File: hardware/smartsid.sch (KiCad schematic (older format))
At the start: 48 parts, among them P1 INPUT, P2 CONTROL, P3 POT2, P4 SOCKET, P5 OUTPUT, U1 GAL16V8, U2 SID2, U3 7812, U4 7809, U5 SID1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

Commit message: Hardware: Added digifix again, rearranged components, rerouted
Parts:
- removed JP8: NR2, Pin_Headers:Pin_Header_Straight_1x02, symbol JUMPER
- removed P2: CONTROL, Pin_Headers:Pin_Header_Straight_1x06, symbol CONN_01X06
- removed R1: 100k, Discret:R1, symbol R_Small
- added C19: 10n, Capacitors_ThroughHole:C_Disc_D3_P2.5, symbol C
- added JP10: NR2, Pin_Headers:Pin_Header_Straight_1x02, symbol JUMPER
- added JP11: INPUT1, Pinheaders:Pin_Header_Straight_1x03, symbol JUMPER3
- added JP8: INPUT2, Pinheaders:Pin_Header_Straight_1x03, symbol JUMPER3
- added P2: CONTROL, Pin_Headers:Pin_Header_Straight_2x03, symbol CONN_02X03
- added R1, R10: 220, Discret:R1, symbol R
- added R9: 100k, Discret:R1, symbol R_Small
- added RV1, RV2: 1M, Potentiometers:Potentiometer_Trimmer-Suntan-TSR-3386C, symbol POT
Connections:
- net labels added: S1IN, S2IN
- wire segments 80 -> 82
- no-connect marks 8 -> 10
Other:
- moved on the sheet: C14, C15, C16, C17, C18, JP9, R2, R3, R4, R5, R6, R7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

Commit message: Hardware: Now using original output circuits instead of opamp
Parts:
- removed C15, C16: 2.2u, Capacitors_ThroughHole:C_Disc_D3_P2.5, symbol C_Small
- removed U7: OPA2132, Housings_DIP:DIP-8_W7.62mm, symbol TL072
- added C15, C20: 1000p, Capacitors_ThroughHole:C_Disc_D3_P2.5, symbol C
- added C16, C21: 470p, Capacitors_ThroughHole:C_Disc_D3_P2.5, symbol C
- added C22: 10u, Capacitors_ThroughHole:C_Radial_D5_L6_P2.5, symbol C
- added Q1, Q2: Q_NPN_BCE, TO_SOT_Packages_THT:TO-92_Inline_Narrow_Oval, symbol Q_NPN_BCE
- added R11: 10k, Discret:R1, symbol R
- added R12: 1k, Discret:R1, symbol R
- C19: value 10n -> 10u; footprint Capacitors_ThroughHole:C_Disc_D3_P2.5 -> Capacitors_ThroughHole:C_Radial_D5_L6_P2.5
- R4: value 47k -> 10k
- R6: value 47k -> 1k
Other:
- moved on the sheet: C13, C14, JP10, JP11, JP8, JP9, R1, R10, R2, R9, RV1, RV2

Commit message: Hardware: Use pin headers instead of dip socket for the sid socket
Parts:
- removed P4: SOCKET, Housings_DIP:DIP-28_W15.24mm, symbol CONN_01X28
- added P4: SOCKET LEFT, Pin_Headers:Pin_Header_Straight_1x14, symbol CONN_01X14
- added P6: SOCKET RIGHT, Pin_Headers:Pin_Header_Straight_1x14, symbol CONN_01X14
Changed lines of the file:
@@
 	1    0    0    -1
 $EndComp
-$Comp
-L CONN_01X28 P4
-U 1 1 56D96DFF
-P 1250 5550
-F 0 "P4" H 1250 7000 50  0000 C CNN
-F 1 "SOCKET" V 1350 5550 50  0000 C CNN
-F 2 "Housings_DIP:DIP-28_W15.24mm" H 1250 5550 60  0001 C CNN
-F 3 "" H 1250 5550 60  0000 C CNN
-	1    1250 5550
-	1    0    0    -1
-$EndComp
-NoConn ~ 1050 4200
-NoConn ~ 1050 4300
-NoConn ~ 1050 4400
-NoConn ~ 1050 4500
-Text Label 1050 4600 2    60   ~ 0
+NoConn ~ 1000 4050
+NoConn ~ 1000 4150
+NoConn ~ 1000 4250
+NoConn ~ 1000 4350
+Text Label 1000 4450 2    60   ~ 0
 ~RES
-Text Label 1050 4700 2    60   ~ 0
+Text Label 1000 4550 2    60   ~ 0
 CLK
-Text Label 1050 4800 2    60   ~ 0
+Text Label 1000 4650 2    60   ~ 0
 RW
-Text Label 1050 4900 2    60   ~ 0
+Text Label 1000 4750 2    60   ~ 0
 ~CS
-Text Label 1050 5000 2    60   ~ 0
+Text Label 1000 4850 2    60   ~ 0
 A0
-Text Label 1050 5100 2    60   ~ 0
+Text Label 1000 4950 2    60   ~ 0
 A1
-Text Label 1050 5200 2    60   ~ 0
+Text Label 1000 5050 2    60   ~ 0
 A2
-Text Label 1050 5300 2    60   ~ 0
+Text Label 1000 5150 2    60   ~ 0
 A3
-Text Label 1050 5400 2    60   ~ 0
+Text Label 1000 5250 2    60   ~ 0
 A4
-Text Label 1050 5600 2    60   ~ 0
+Text Label 1000 5700 2    60   ~ 0
 D0
-Text Label 1050 5700 2    60   ~ 0
+Text Label 1000 5800 2    60   ~ 0
 D1
-Text Label 1050 5800 2    60   ~ 0
+Text Label 1000 5900 2    60   ~ 0
 D2
-Text Label 1050 5900 2    60   ~ 0
+Text Label 1000 6000 2    60   ~ 0
 D3
-Text Label 1050 6000 2    60   ~ 0
+Text Label 1000 6100 2    60   ~ 0
 D4
-Text Label 1050 6100 2    60   ~ 0
+Text Label 1000 6200 2    60   ~ 0
 D5
-Text Label 1050 6200 2    60   ~ 0
+Text Label 1000 6300 2    60   ~ 0
 D6
-Text Label 1050 6300 2    60   ~ 0
+Text Label 1000 6400 2    60   ~ 0
 D7
-Text Label 1050 6400 2    60   ~ 0
+Text Label 1000 6500 2    60   ~ 0
 POTY
-Text Label 1050 6500 2    60   ~ 0
+Text Label 1000 6600 2    60   ~ 0
 POTX
 $Comp
 L VCC #PWR08
 U 1 1 56D974B1
-P 800 6600
-F 0 "#PWR08" H 800 6450 50  0001 C CNN
-F 1 "VCC" H 800 6750 50  0000 C CNN
-F 2 "" H 800 6600 60  0000 C CNN
-F 3 "" H 800 6600 60  0000 C CNN
-	1    800  6600
+P 750 6700
+F 0 "#PWR08" H 750 6550 50  0001 C CNN
+F 1 "VCC" H 750 6850 50  0000 C CNN
+F 2 "" H 750 6700 60  0000 C CNN
+F 3 "" H 750 6700 60  0000 C CNN
+	1    750  6700
 	0    -1   -1   0
 $EndComp
@@
 L GND #PWR09
 U 1 1 56D9751E
-P 850 5500
-F 0 "#PWR09" H 850 5250 50  0001 C CNN
-F 1 "GND" H 850 5350 50  0000 C CNN
-F 2 "" H 850 5500 60  0000 C CNN
-F 3 "" H 850 5500 60  0000 C CNN
-	1    850  5500
+P 800 5350
+F 0 "#PWR09" H 800 5100 50  0001 C CNN
+F 1 "GND" H 800 5200 50  0000 C CNN
+F 2 "" H 800 5350 60  0000 C CNN
+F 3 "" H 800 5350 60  0000 C CNN
+	1    800  5350
 	0    1    1    0
 $EndComp
-NoConn ~ 1050 6700
-NoConn ~ 1050 6800
+NoConn ~ 1000 6800
+NoConn ~ 1000 6900
 $Comp
 L VDD #PWR010
 U 1 1 56D9CAE7
-P 1050 6900
-F 0 "#PWR010" H 1050 6750 50  0001 C CNN
-F 1 "VDD" H 1050 7050 50  0000 C CNN
-F 2 "" H 1050 6900 60  0000 C CNN
-F 3 "" H 1050 6900 60  0000 C CNN
-	1    1050 6900
+P 1000 7000
+F 0 "#PWR010" H 1000 6850 50  0001 C CNN
+F 1 "VDD" H 1000 7150 50  0000 C CNN
+F 2 "" H 1000 7000 60  0000 C CNN
+F 3 "" H 1000 7000 60  0000 C CNN
+	1    1000 7000
 	0    -1   -1   0
 $EndComp
@@
 Connection ~ 4150 7100
 Wire Wire Line
-	850  5500 1050 5500
-Wire Wire Line
-	800  6600 1050 6600
+	800  5350 1000 5350
+Wire Wire Line
+	750  6700 1000 6700
 Wire Wire Line
 	7050 1400 6500 1400
@@
 $EndComp
 Connection ~ 6550 4450
+$Comp
+L CONN_01X14 P4
+U 1 1 56E7E66F
+P 1200 4700
+F 0 "P4" H 1200 5450 50  0000 C CNN
+F 1 "SOCKET LEFT" V 1300 4700 50  0000 C CNN
+F 2 "Pin_Headers:Pin_Header_Straight_1x14" H 1200 4700 60  0001 C CNN
+F 3 "" H 1200 4700 60  0000 C CNN
+	1    1200 4700
+	1    0    0    -1
+$EndComp
+$Comp
+L CONN_01X14 P6
+U 1 1 56E7EC84
+P 1200 6350
+F 0 "P6" H 1200 7100 50  0000 C CNN
+F 1 "SOCKET RIGHT" V 1300 6350 50  0000 C CNN
+F 2 "Pin_Headers:Pin_Header_Straight_1x14" H 1200 6350 60  0001 C CNN
+F 3 "" H 1200 6350 60  0000 C CNN
+	1    1200 6350
+	1    0    0    -1
+$EndComp
 $EndSCHEMATC

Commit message: Hardware: Rearranged components, made control lines usable with jumpers
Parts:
- removed P2: CONTROL, Pin_Headers:Pin_Header_Straight_2x03, symbol CONN_02X03
- added P2: CONTROL, Pin_Headers:Pin_Header_Straight_2x06, symbol CONN_02X06
- JP10, JP9: footprint Pin_Headers:Pin_Header_Straight_1x02 -> Pinheaders:Pin_Header_Straight_1x02
- P4, P6: footprint Pin_Headers:Pin_Header_Straight_1x14 -> Pinheaders:Pin_Header_Straight_1x14
- RV1, RV2: footprint Potentiometers:Potentiometer_Trimmer-Suntan-TSR-3386C -> Potentiometers:Potentiometer_Bourns_3296W_3-8Zoll_Inline_ScrewUp
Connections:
- wire segments 82 -> 83

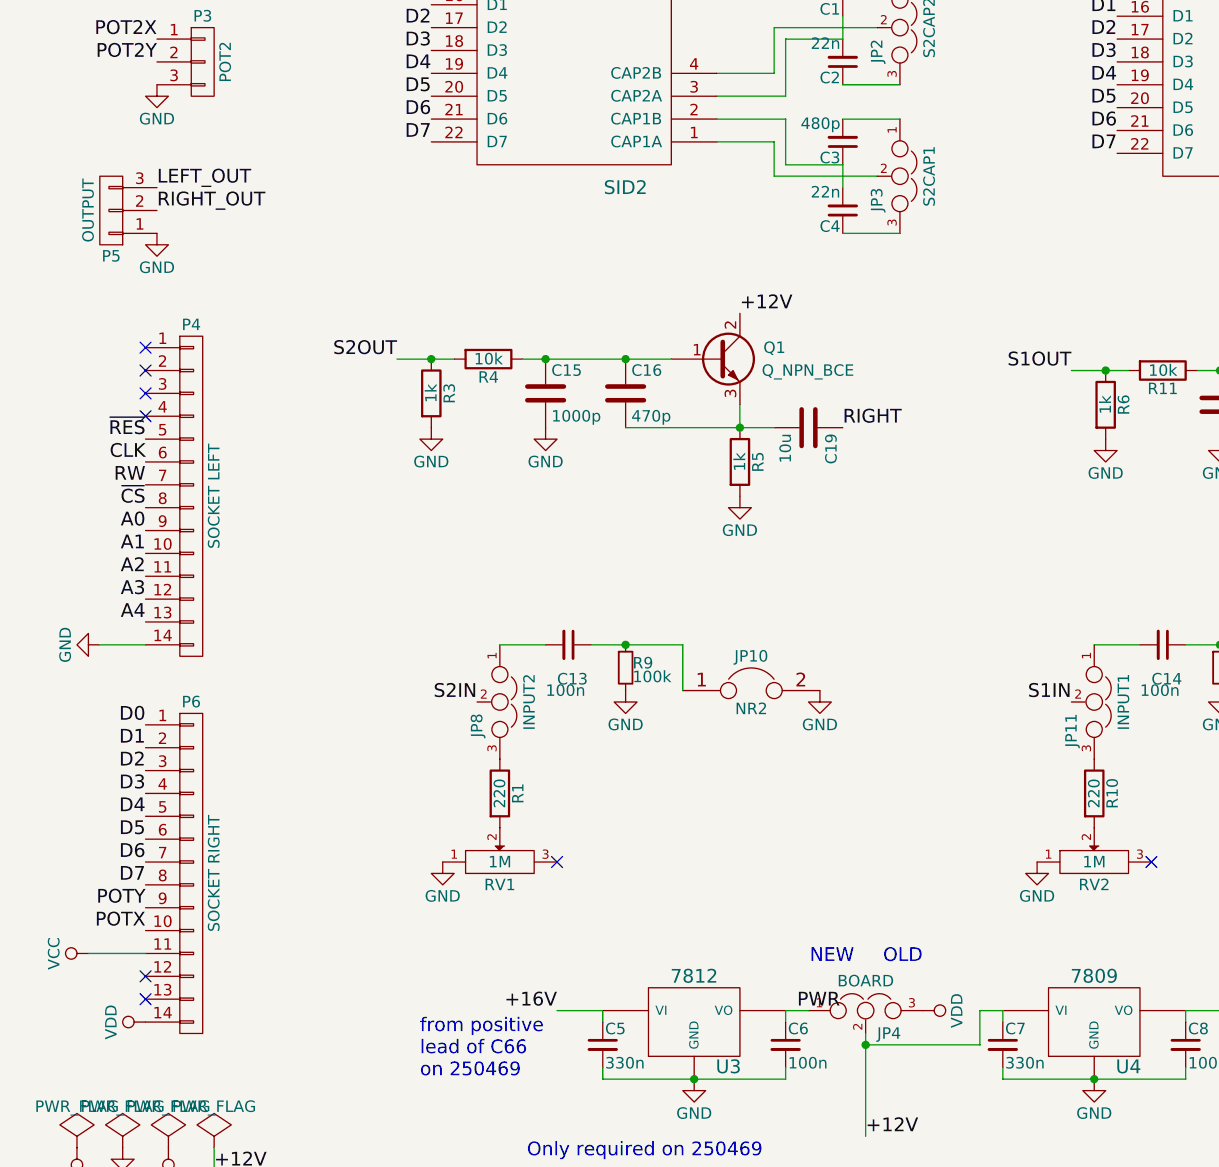
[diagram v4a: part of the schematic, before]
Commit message: Hardware: Added optional mono mixing into existing output circuit
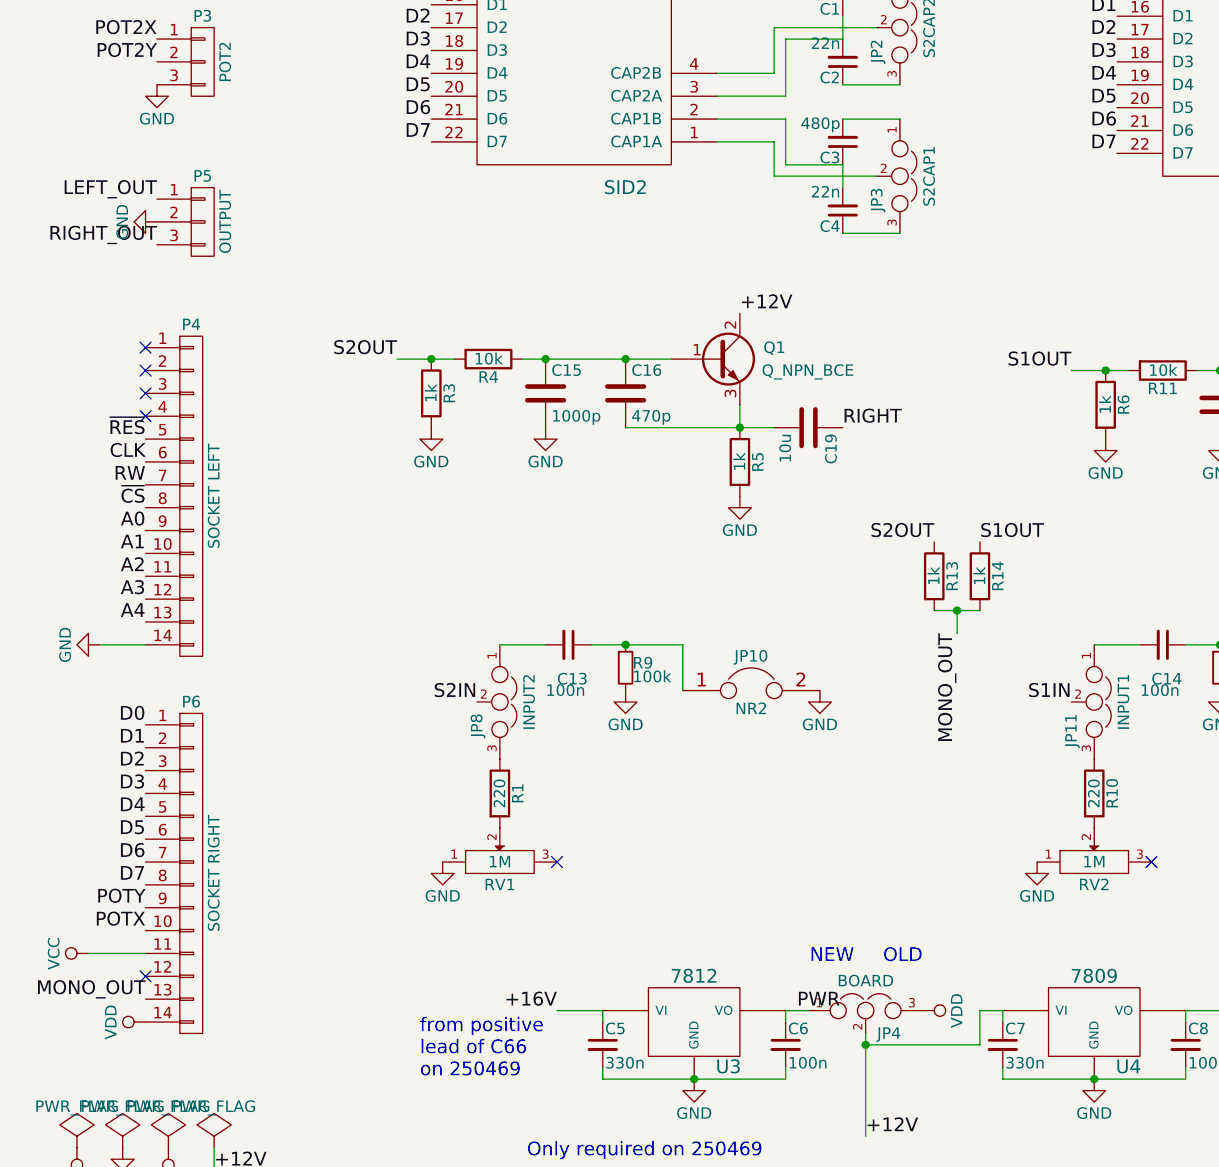
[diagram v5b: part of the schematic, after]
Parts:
- added R13, R14: 1k, Discret:R1, symbol R
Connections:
- net GND: now also P5.2 (P2); no longer P5.1 (P1)
- net LEFT_OUT: now also P5.1 (P1); no longer P5.3 (P3)
- net RIGHT_OUT: now also P5.3 (P3); no longer P5.2 (P2)
- net S1OUT: now also R14.1
- net S2OUT: now also R13.1
- net MONO_OUT: now reaches P6.13 (P13)
- net MONO_OUT: now also R13.2, R14.2
- no-connect marks 10 -> 9
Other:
- moved on the sheet: P5
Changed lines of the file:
@@
 $EndComp
 NoConn ~ 1000 6800
-NoConn ~ 1000 6900
 $Comp
 L VDD #PWR09
@@
 L CONN_01X03 P5
 U 1 1 56DA6151
-P 850 3450
-F 0 "P5" H 850 3650 50  0000 C CNN
-F 1 "OUTPUT" V 950 3450 50  0000 C CNN
-F 2 "Pinheaders:Pin_Header_Straight_1x03" H 850 3450 60  0001 C CNN
-F 3 "" H 850 3450 60  0000 C CNN
-	1    850  3450
-	-1   0    0    1
+P 1250 3500
+F 0 "P5" H 1250 3700 50  0000 C CNN
+F 1 "OUTPUT" V 1350 3500 50  0000 C CNN
+F 2 "Pinheaders:Pin_Header_Straight_1x03" H 1250 3500 60  0001 C CNN
+F 3 "" H 1250 3500 60  0000 C CNN
+	1    1250 3500
+	1    0    0    -1
 $EndComp
 $Comp
 L GND #PWR014
 U 1 1 56DA641A
-P 1050 3550
-F 0 "#PWR014" H 1050 3300 50  0001 C CNN
-F 1 "GND" H 1050 3400 50  0000 C CNN
-F 2 "" H 1050 3550 60  0000 C CNN
-F 3 "" H 1050 3550 60  0000 C CNN
-	1    1050 3550
-	1    0    0    -1
+P 1050 3500
+F 0 "#PWR014" H 1050 3250 50  0001 C CNN
+F 1 "GND" H 1050 3350 50  0000 C CNN
+F 2 "" H 1050 3500 60  0000 C CNN
+F 3 "" H 1050 3500 60  0000 C CNN
+	1    1050 3500
+	0    1    1    0
 $EndComp
 Text Label 4050 4400 0    60   ~ 0
@@
 Text Label 8650 5450 2    60   ~ 0
 LEFT
-Text Label 1050 3350 0    60   ~ 0
+Text Label 1050 3400 2    60   ~ 0
 LEFT_OUT
-Text Label 1050 3450 0    60   ~ 0
+Text Label 1050 3600 2    60   ~ 0
 RIGHT_OUT
 $Comp
@@
 	1    0    0    -1
 $EndComp
+Text Label 4450 4900 2    60   ~ 0
+S2OUT
+Text Label 4650 4900 0    60   ~ 0
+S1OUT
+$Comp
+L R R13
+U 1 1 56EC71A3
+P 4450 5050
+F 0 "R13" V 4530 5050 50  0000 C CNN
+F 1 "1k" V 4450 5050 50  0000 C CNN
+F 2 "Discret:R1" V 4380 5050 50  0001 C CNN
+F 3 "" H 4450 5050 50  0000 C CNN
+	1    4450 5050
+	1    0    0    -1
+$EndComp
+$Comp
+L R R14
+U 1 1 56EC7384
+P 4650 5050
+F 0 "R14" V 4730 5050 50  0000 C CNN
+F 1 "1k" V 4650 5050 50  0000 C CNN
+F 2 "Discret:R1" V 4580 5050 50  0001 C CNN
+F 3 "" H 4650 5050 50  0000 C CNN
+	1    4650 5050
+	1    0    0    -1
+$EndComp
+Wire Wire Line
+	4450 5200 4650 5200
+Wire Wire Line
+	4550 5200 4550 5300
+Connection ~ 4550 5200
+Text Label 4550 5300 3    60   ~ 0
+MONO_OUT
+Text Label 1000 6900 2    60   ~ 0
+MONO_OUT
 $EndSCHEMATC
